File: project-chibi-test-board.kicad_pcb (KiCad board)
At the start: 4 copper layers, 104.1 x 134.6 mm, 226 parts, among them J1 Conn_01x04, J10 Conn_01x02, J11 Conn_01x02, J12 Conn_02x06_Top_Bottom, J13 Conn_02x06_Top_Bottom, J14 Conn_02x06_Top_Bottom, J15 Conn_02x06_Top_Bottom, J16 Conn_01x02, J17 Conn_01x02, J18 Conn_Coaxial, J19 Conn_Coaxial, J2 Conn_Coaxial, J20 Conn_01x03, J21 Conn_01x03, J22 Conn_01x04, J23 USB_B_Micro, J24 Conn_01x06, J25 Conn_01x04, J26 Conn_Coaxial, J27 Conn_Coaxial, J28 Conn_01x03, J29 Conn_01x03, J3 Conn_Coaxial, J30 Conn_01x02, J31 Conn_01x02, J32 Conn_02x06_Top_Bottom, J33 Conn_02x06_Top_Bottom, J34 Conn_02x06_Top_Bottom, J35 Conn_02x06_Top_Bottom, J36 Conn_02x06_Top_Bottom, J37 Conn_02x06_Top_Bottom, J38 Conn_02x06_Top_Bottom, J39 Conn_02x06_Top_Bottom, J4 Conn_01x03, J40 Conn_01x02, J41 Conn_01x02, J42 Conn_Coaxial, J43 Conn_Coaxial, J44 Conn_01x04, J45 Conn_01x03, J46 Conn_01x03, J47 Conn_01x06, J48 Conn_01x02, J49 Conn_01x02, J5 Conn_01x03, J50 Conn_01x02, J51 Conn_01x02, J52 Conn_01x02, J6 Conn_02x06_Top_Bottom, J7 Conn_02x06_Top_Bottom, J8 Conn_02x06_Top_Bottom, J9 Conn_01x06, SW1 SW_DIP_x08, SW2 SW_DIP_x08, U1 40 MHz, U10 5M240ZT144C5N, U11 5M1270ZF256C5N, U2 2.048 MHz, U3 5M40ZE64C5N, U4 5M2210ZF256C5N, U5 93LC56BT-OT, U6 5M240ZT144C5N, U7 LM1117-3.3, U8 LM1117-1.8, U9 FT232H, Y1 12 MHz

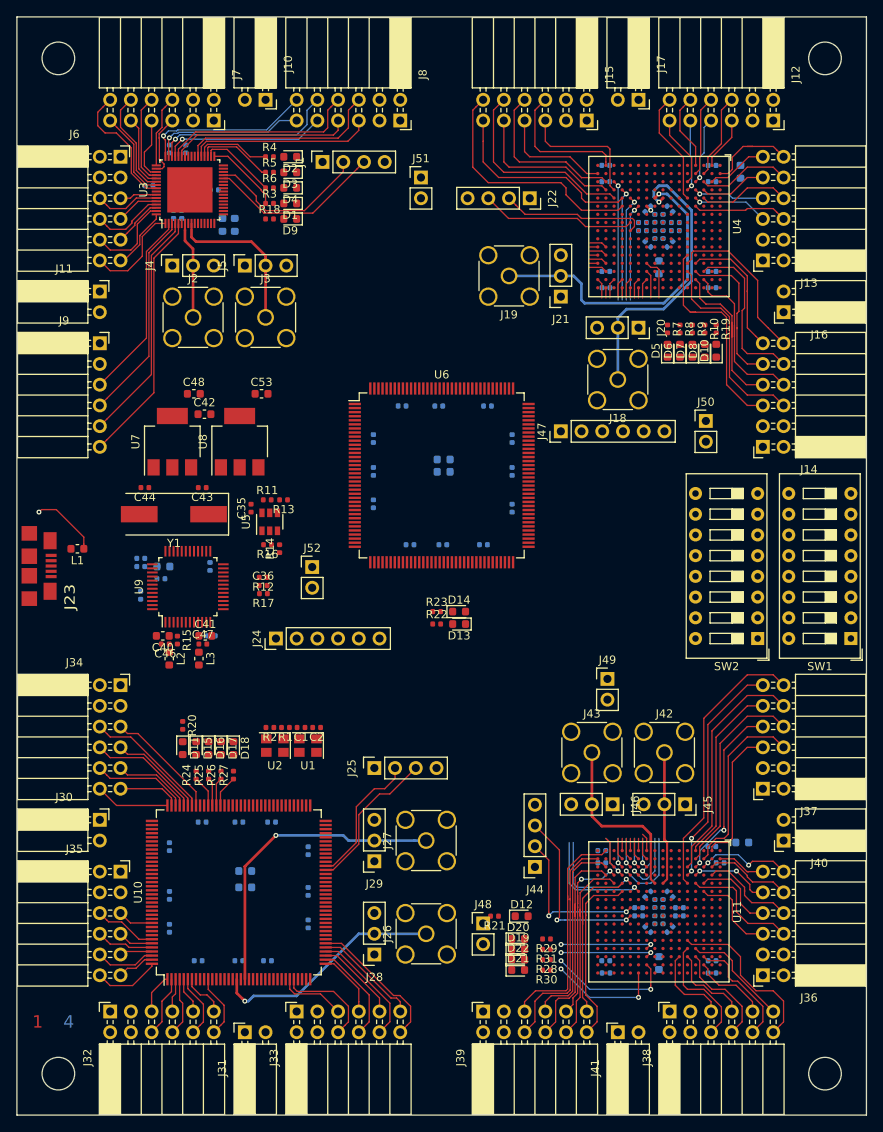
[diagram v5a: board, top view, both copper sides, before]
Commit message: massive mux pin reswap
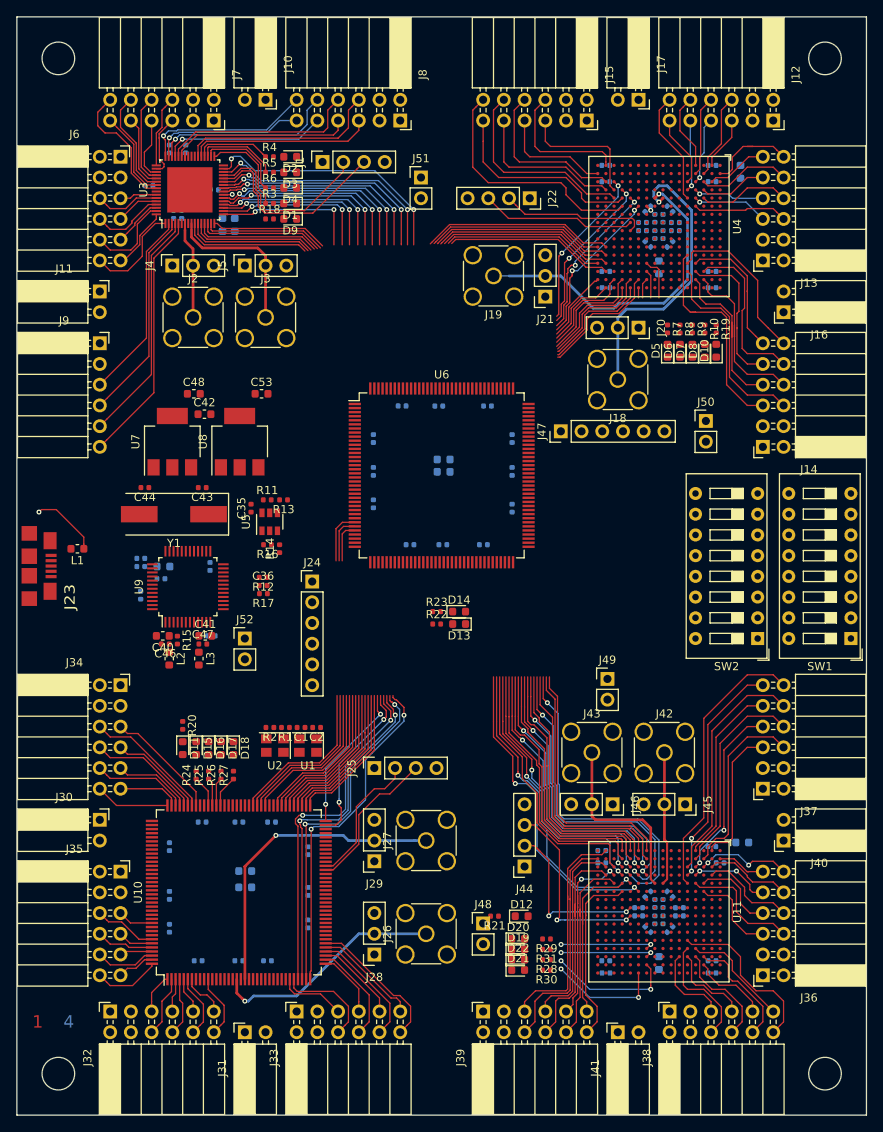
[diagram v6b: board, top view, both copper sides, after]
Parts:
- moved J52 12.0 mm to (78.7, 127.0)
- moved J24 8.28 mm to (87.0, 120.0), turned to 0 degrees
- moved J19 1.91 mm to (109.2, 82.5)
- moved J21 1.91 mm to (115.6, 85.1)
- moved J44 1.27 mm to (113.0, 154.9)
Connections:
- net Net-(J24-Pad2) renamed /jtag-iface/MUX_TMS
- net Net-(J24-Pad3) renamed /jtag-iface/MUX_TCK
- net Net-(J24-Pad4) renamed /jtag-iface/MUX_TDI
- net Net-(J24-Pad5) renamed /jtag-iface/MUX_TDO
- U6 pad 1: /tgt-4x6/ACBUS6 -> /tgt-4x6/JTAG_TCK
- U6 pad 107: /tgt-13x20/ACBUS4 -> /tgt-13x20/ADBUS0
- U6 pad 108: /tgt-13x20/ACBUS3 -> /tgt-13x20/ADBUS1
- U6 pad 109: /tgt-13x20/ACBUS0 -> /tgt-13x20/ADBUS2
- U6 pad 110: /tgt-13x20/ACBUS1 -> /tgt-13x20/ADBUS3
- U6 pad 111: /tgt-13x20/ACBUS2 -> /tgt-13x20/ADBUS4
- U6 pad 112: /tgt-13x20/JTAG_TMS -> /tgt-13x20/ADBUS5
- U6 pad 113: /tgt-13x20/JTAG_TCK -> /tgt-13x20/ADBUS7
- U6 pad 117: /tgt-13x20/ADBUS7 -> /tgt-13x20/JTAG_TDI
- U6 pad 118: /tgt-13x20/ADBUS3 -> /tgt-13x20/JTAG_TDO
- U6 pad 119: /tgt-13x20/ADBUS4 -> /tgt-13x20/JTAG_TMS
- U6 pad 120: /tgt-13x20/ADBUS5 -> /tgt-13x20/JTAG_TCK
- U6 pad 121: /tgt-13x20/ADBUS0 -> /tgt-13x20/ACBUS0
- U6 pad 122: /tgt-13x20/ADBUS1 -> /tgt-13x20/ACBUS1
- U6 pad 123: /tgt-13x20/ADBUS2 -> /tgt-13x20/ACBUS2
- U6 pad 124: /tgt-13x20/JTAG_TDO -> /tgt-13x20/ACBUS3
- U6 pad 125: /tgt-13x20/JTAG_TDI -> /tgt-13x20/ACBUS4
- U6 pad 129: /tgt-4x6/ACBUS3 -> /tgt-13x20/ACBUS6
- U6 pad 130: /tgt-13x20/ACBUS6 -> /tgt-4x6/ACBUS5
- U6 pad 131: /tgt-4x6/ADBUS6 -> /tgt-4x6/ACBUS6
- U6 pad 132: /tgt-4x6/ACBUS0 -> /tgt-4x6/ACBUS3
- U6 pad 133: /tgt-4x6/ACBUS1 -> /tgt-4x6/ACBUS4
- U6 pad 134: /tgt-4x6/ACBUS2 -> /tgt-4x6/ACBUS0
- U6 pad 138: /tgt-4x6/ADBUS7 -> /tgt-4x6/ACBUS1
- U6 pad 139: /tgt-4x6/ADBUS1 -> /tgt-4x6/ACBUS2
- U6 pad 142: /tgt-4x6/ADBUS2 -> /tgt-4x6/ADBUS6
- U6 pad 143: /tgt-4x6/ADBUS3 -> /tgt-4x6/ADBUS7
- U6 pad 144: /tgt-4x6/ADBUS0 -> /tgt-4x6/JTAG_TDO
- U6 pad 2: /tgt-4x6/ACBUS4 -> /tgt-4x6/JTAG_TDI
- U6 pad 3: /tgt-4x6/ACBUS5 -> /tgt-4x6/JTAG_TMS
- U6 pad 30: /tgt-7x12/ADBUS5 -> /tgt-7x12/ADBUS0
- U6 pad 31: /tgt-7x12/ADBUS7 -> /tgt-7x12/ADBUS1
- U6 pad 32: /tgt-7x12/ADBUS6 -> /tgt-7x12/ADBUS2
- U6 pad 37: /tgt-7x12/ACBUS6 -> /tgt-7x12/ADBUS3
- U6 pad 38: /tgt-7x12/ACBUS5 -> /tgt-7x12/ADBUS4
- U6 pad 39: /tgt-7x12/ADBUS4 -> /tgt-7x12/ADBUS5
- U6 pad 4: /tgt-4x6/JTAG_TDI -> /tgt-4x6/ADBUS3
- U6 pad 40: /tgt-7x12/JTAG_TDO -> /tgt-7x12/ADBUS6
- U6 pad 41: /tgt-7x12/JTAG_TDI -> /tgt-7x12/ADBUS7
- U6 pad 42: /tgt-7x12/ADBUS0 -> /tgt-7x12/ACBUS0
- U6 pad 43: /tgt-7x12/JTAG_TCK -> /tgt-7x12/ACBUS1
- U6 pad 44: /tgt-7x12/JTAG_TMS -> /tgt-7x12/ACBUS2
- U6 pad 45: /tgt-7x12/ADBUS3 -> /tgt-7x12/ACBUS3
- U6 pad 48: /tgt-7x12/ADBUS2 -> /tgt-7x12/ACBUS4
- U6 pad 49: /tgt-7x12/ADBUS1 -> /tgt-7x12/ACBUS5
- U6 pad 5: /tgt-4x6/JTAG_TDO -> /tgt-4x6/ADBUS2
- U6 pad 50: /tgt-7x12/ACBUS4 -> /tgt-7x12/ACBUS6
- U6 pad 51: /tgt-7x12/ACBUS3 -> /tgt-7x12/JTAG_TMS
- U6 pad 52: /tgt-7x12/ACBUS2 -> /tgt-7x12/JTAG_TDI
- U6 pad 53: /tgt-7x12/ACBUS0 -> /tgt-7x12/JTAG_TCK
- U6 pad 55: /tgt-7x12/ACBUS1 -> /tgt-7x12/JTAG_TDO
- U6 pad 6: /tgt-4x6/JTAG_TMS -> /tgt-4x6/ADBUS1
- U6 pad 60: /tgt-10x16/ADBUS6 -> /tgt-10x16/JTAG_TDI
- U6 pad 61: /tgt-10x16/ADBUS5 -> /tgt-10x16/JTAG_TDO
- U6 pad 62: /tgt-10x16/ADBUS4 -> /tgt-10x16/JTAG_TCK
- U6 pad 63: /tgt-10x16/ADBUS3 -> /tgt-10x16/JTAG_TMS
- U6 pad 66: /tgt-10x16/ACBUS5 -> /tgt-10x16/ACBUS3
- U6 pad 67: /tgt-10x16/ACBUS4 -> /tgt-10x16/ADBUS7
- U6 pad 68: /tgt-10x16/ADBUS7 -> /tgt-10x16/ACBUS2
- U6 pad 69: /tgt-10x16/ADBUS0 -> /tgt-10x16/ADBUS6
- U6 pad 7: /tgt-4x6/JTAG_TCK -> /tgt-4x6/ADBUS0
- U6 pad 70: /tgt-10x16/ACBUS6 -> /tgt-10x16/ACBUS1
- U6 pad 71: /tgt-10x16/ACBUS3 -> /tgt-10x16/ADBUS5
- U6 pad 72: /tgt-10x16/ACBUS2 -> /tgt-10x16/ACBUS0
- U6 pad 73: /tgt-10x16/ACBUS1 -> /tgt-10x16/ADBUS4
- U6 pad 74: /tgt-10x16/ACBUS0 -> /tgt-10x16/ACBUS4
- U6 pad 75: /tgt-10x16/JTAG_TMS -> /tgt-10x16/ADBUS3
- U6 pad 76: /tgt-10x16/JTAG_TDO -> /tgt-10x16/ACBUS5
- U6 pad 77: /tgt-10x16/JTAG_TDI -> /tgt-10x16/ADBUS2
- U6 pad 78: /tgt-10x16/JTAG_TCK -> /tgt-10x16/ACBUS6
- U6 pad 79: /tgt-10x16/ADBUS2 -> /tgt-10x16/ADBUS1
- U6 pad 80: /tgt-10x16/ADBUS1 -> /tgt-10x16/ADBUS0
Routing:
- net /tgt-7x12/JTAG_TMS: track 0.00 -> 43.0 mm, vias 0 -> 2
- net /tgt-7x12/JTAG_TDI: track 0.00 -> 42.9 mm, vias 0 -> 2
- net /tgt-7x12/JTAG_TCK: track 0.00 -> 42.5 mm, vias 0 -> 2
- net /tgt-7x12/JTAG_TDO: track 0.00 -> 42.0 mm, vias 0 -> 2
- net /tgt-4x6/ACBUS5: track 0.00 -> 31.5 mm, vias 0 -> 2
- net /tgt-10x16/ACBUS5: track 8.04 -> 39.1 mm, vias 1 -> 2
- net /tgt-10x16/ACBUS6: track 10.2 -> 41.2 mm, vias 1 -> 2
- net /tgt-10x16/ACBUS4: track 5.12 -> 36.0 mm, vias 1 -> 2
- net /tgt-10x16/ACBUS0: track 3.71 -> 34.5 mm, vias 1 -> 2
- net /tgt-10x16/ACBUS1: track 3.71 -> 34.1 mm, vias 1 -> 2
- net /tgt-10x16/ADBUS6: track 1.50 -> 31.4 mm
- net /tgt-10x16/ACBUS2: track 3.71 -> 33.6 mm, vias 1 -> 2
- net /tgt-4x6/ACBUS6: track 0.00 -> 29.7 mm, vias 0 -> 2
- net /tgt-10x16/ADBUS4: track 1.50 -> 31.2 mm
- net /tgt-10x16/ADBUS5: track 2.71 -> 32.3 mm
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
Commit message: work on qfp decoupling; one bga decoupling
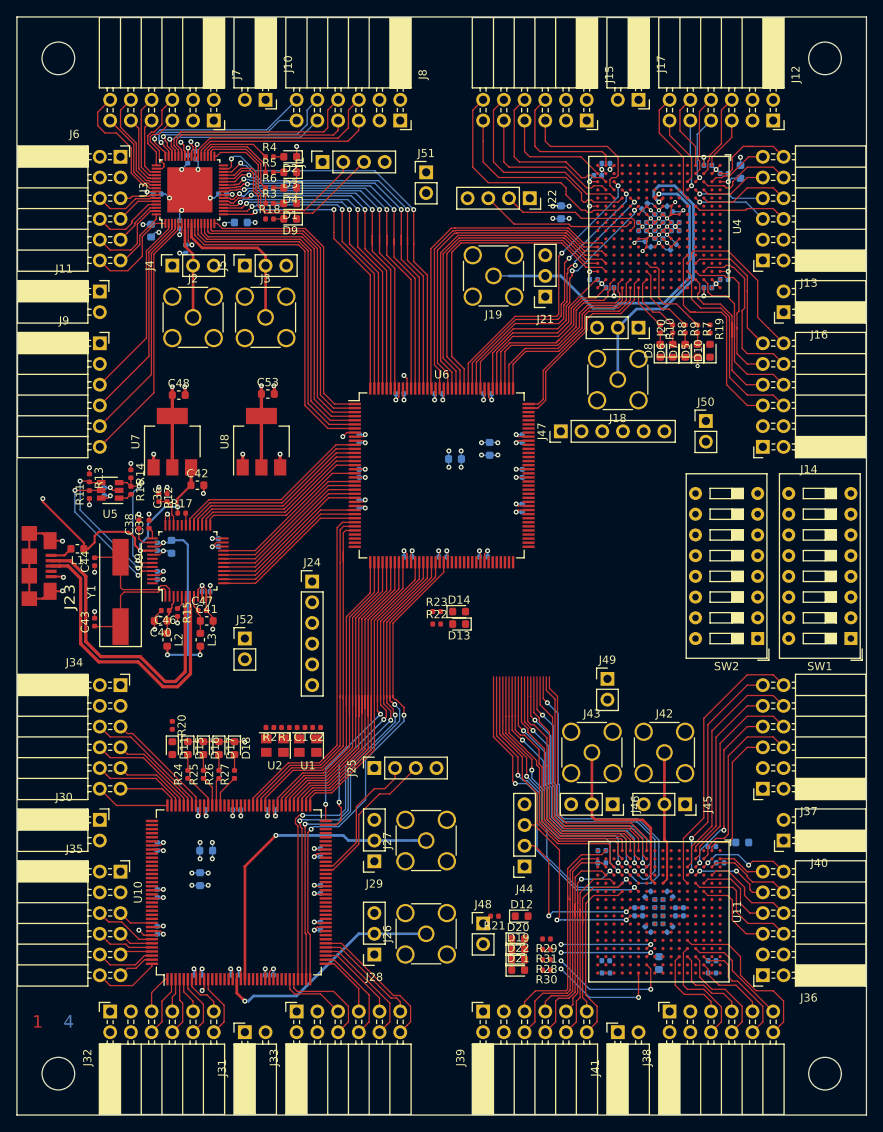
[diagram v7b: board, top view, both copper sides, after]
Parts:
- C35: moved to B.Cu
- C37, C38: moved to F.Cu
- moved R13 23.9 mm to (59.7, 107.3), turned to 270 degrees
- moved R11 21.8 mm to (59.7, 109.3), turned to 90 degrees
- moved C43 21.1 mm to (60.3, 125.0), turned to 90 degrees
- moved R14 20.4 mm to (64.8, 106.8), turned to 270 degrees
- moved U5 19.9 mm to (62.2, 108.8), turned to 180 degrees
- moved C35 18.1 mm to (61.5, 109.0)
- moved R16 18.0 mm to (64.8, 108.8), turned to 270 degrees
- moved R12 16.1 mm to (68.2, 109.7), turned to 270 degrees
- moved C36 16.0 mm to (69.2, 109.7), turned to 90 degrees
- moved R17 14.1 mm to (71.0, 111.6), turned to 0 degrees
- moved C99 13.8 mm to (117.5, 74.8), turned to 90 degrees
- moved Y1 11.6 mm to (63.5, 121.3), turned to 90 degrees
- moved C44 11.0 mm to (60.3, 117.6), turned to 90 degrees
- moved C98 10.3 mm to (67.2, 77.0)
- moved C42 8.75 mm to (72.9, 108.2)
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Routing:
- net GND: track 0.00 -> 211.7 mm, vias 0 -> 89
- net +3V3: track 1.10 -> 103.6 mm, vias 1 -> 47
- net +1V8: track 0.71 -> 50.2 mm, vias 1 -> 21
- net /jtag-iface/USB_P: track 0.00 -> 38.1 mm
- net /jtag-iface/USB_N: track 0.00 -> 37.0 mm
- net /tgt-4x6/ADBUS0: track 15.8 -> 42.0 mm
- net /tgt-4x6/ADBUS1: track 15.6 -> 41.2 mm
- net /jtag-iface/FTDI_VCCD: track 0.00 -> 25.3 mm, vias 0 -> 3
- net +5V: track 547.9 -> 573.0 mm, vias 1 -> 3
- net /tgt-4x6/ADBUS2: track 15.5 -> 40.4 mm
- net /jtag-iface/ACBUS6: track 0.00 -> 24.8 mm
- net /tgt-4x6/ADBUS3: track 15.4 -> 39.7 mm
- net /jtag-iface/ACBUS5: track 0.00 -> 24.1 mm
- net /tgt-4x6/JTAG_TMS: track 15.3 -> 38.9 mm
- net /jtag-iface/ACBUS4: track 0.00 -> 23.4 mm
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
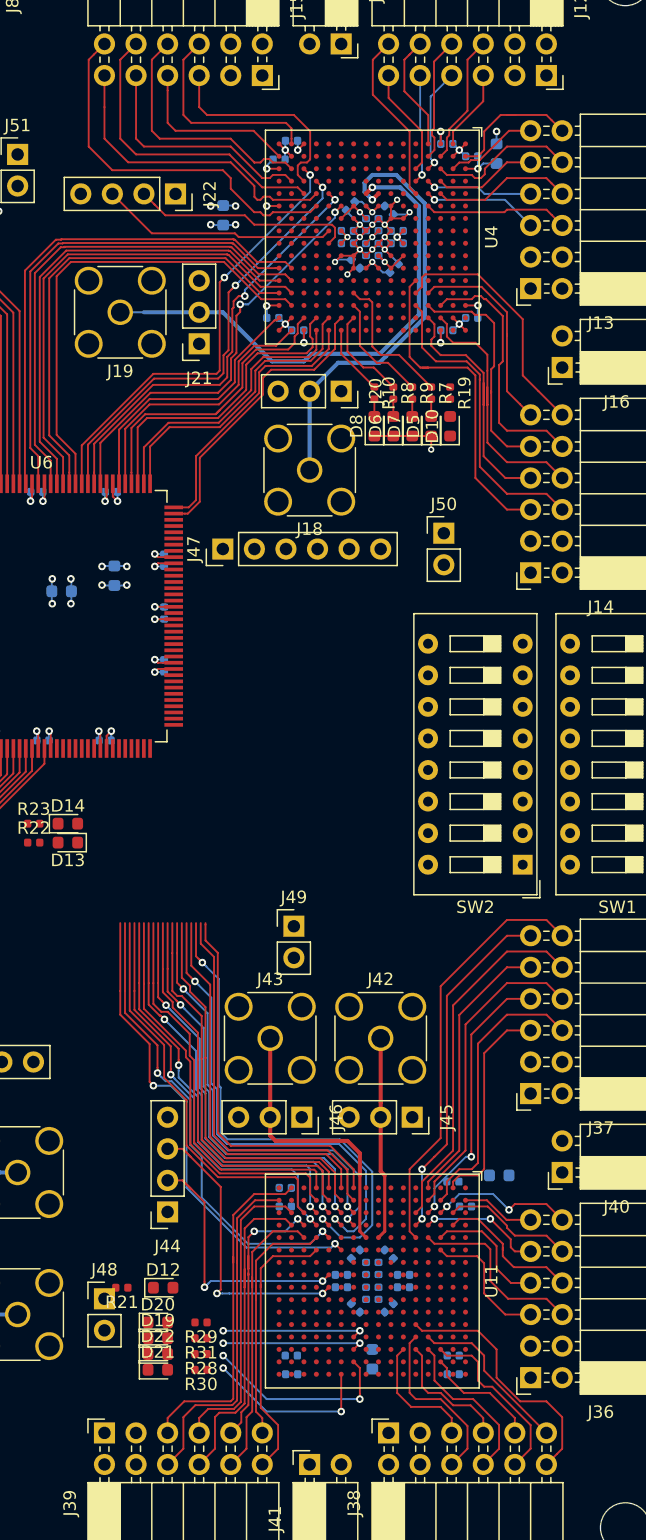
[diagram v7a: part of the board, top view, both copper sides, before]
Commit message: most routing done except leds; oscillators
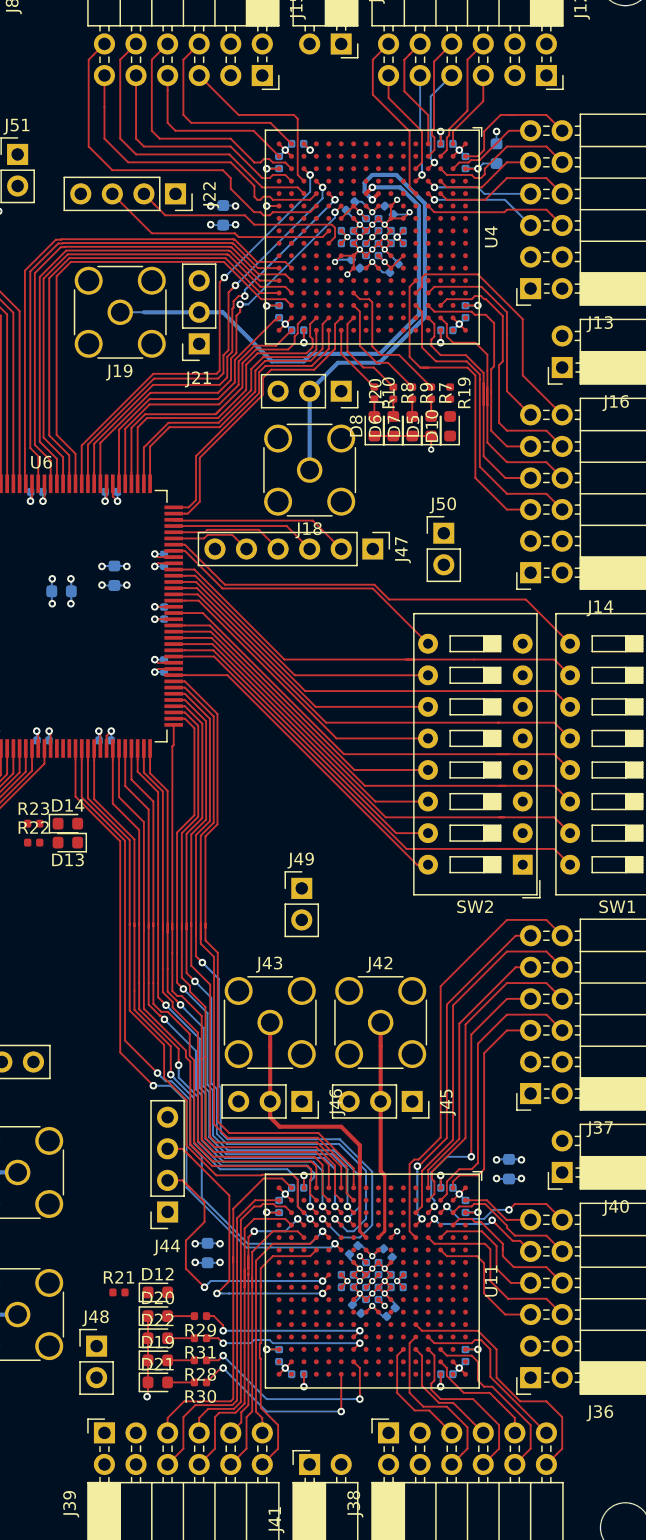
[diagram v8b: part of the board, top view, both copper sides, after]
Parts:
- moved C103 15.8 mm to (116.2, 158.2)
- moved J47 12.1 mm to (129.5, 101.6), turned to 270 degrees
- moved J48 3.86 mm to (107.3, 165.7)
- moved J49 3.11 mm to (123.8, 128.9)
- moved D19 1.78 mm to (112.2, 166.9)
- moved D22 1.27 mm to (112.2, 165.1)
- moved J42 1.27 mm to (130.2, 139.7)
- moved J43 1.27 mm to (121.3, 139.7)
- moved J45 1.27 mm to (132.7, 146.1)
- moved J46 1.27 mm to (123.8, 146.1)
- moved R30 1.02 mm to (115.7, 168.7)
- moved D21 1.02 mm to (112.2, 168.7)
- moved C77 1.00 mm to (123.5, 153.0)
- moved C83 0.99 mm to (137.0, 166.5), turned to 270 degrees
- moved C92 0.98 mm to (122.0, 166.5), turned to 270 degrees
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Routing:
- net GND: track 211.7 -> 266.7 mm, vias 89 -> 107
- net Net-(SW1-Pad16): track 0.00 -> 40.1 mm
- net Net-(SW1-Pad15): track 0.00 -> 38.6 mm
- net Net-(SW1-Pad14): track 0.00 -> 38.1 mm
- net Net-(SW1-Pad13): track 0.00 -> 38.0 mm
- net Net-(SW1-Pad12): track 0.00 -> 36.8 mm
- net Net-(SW1-Pad11): track 0.00 -> 36.8 mm
- net Net-(SW1-Pad10): track 0.00 -> 36.1 mm
- net Net-(SW1-Pad9): track 0.00 -> 35.2 mm
- net +3V3: track 103.6 -> 135.9 mm, vias 47 -> 61
- net Net-(SW2-Pad16): track 0.00 -> 26.8 mm
- net Net-(SW2-Pad15): track 0.00 -> 26.6 mm
- net Net-(SW2-Pad14): track 0.00 -> 25.9 mm
- net Net-(SW2-Pad13): track 0.00 -> 25.3 mm
- net Net-(SW2-Pad12): track 0.00 -> 25.1 mm
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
